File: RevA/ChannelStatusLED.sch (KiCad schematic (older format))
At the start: 6 parts, among them Q1 MBT3946DW1T1, Q2 MBT3946DW1T1, U1 RAx4_4 1K, U2 RAx4_4 1K

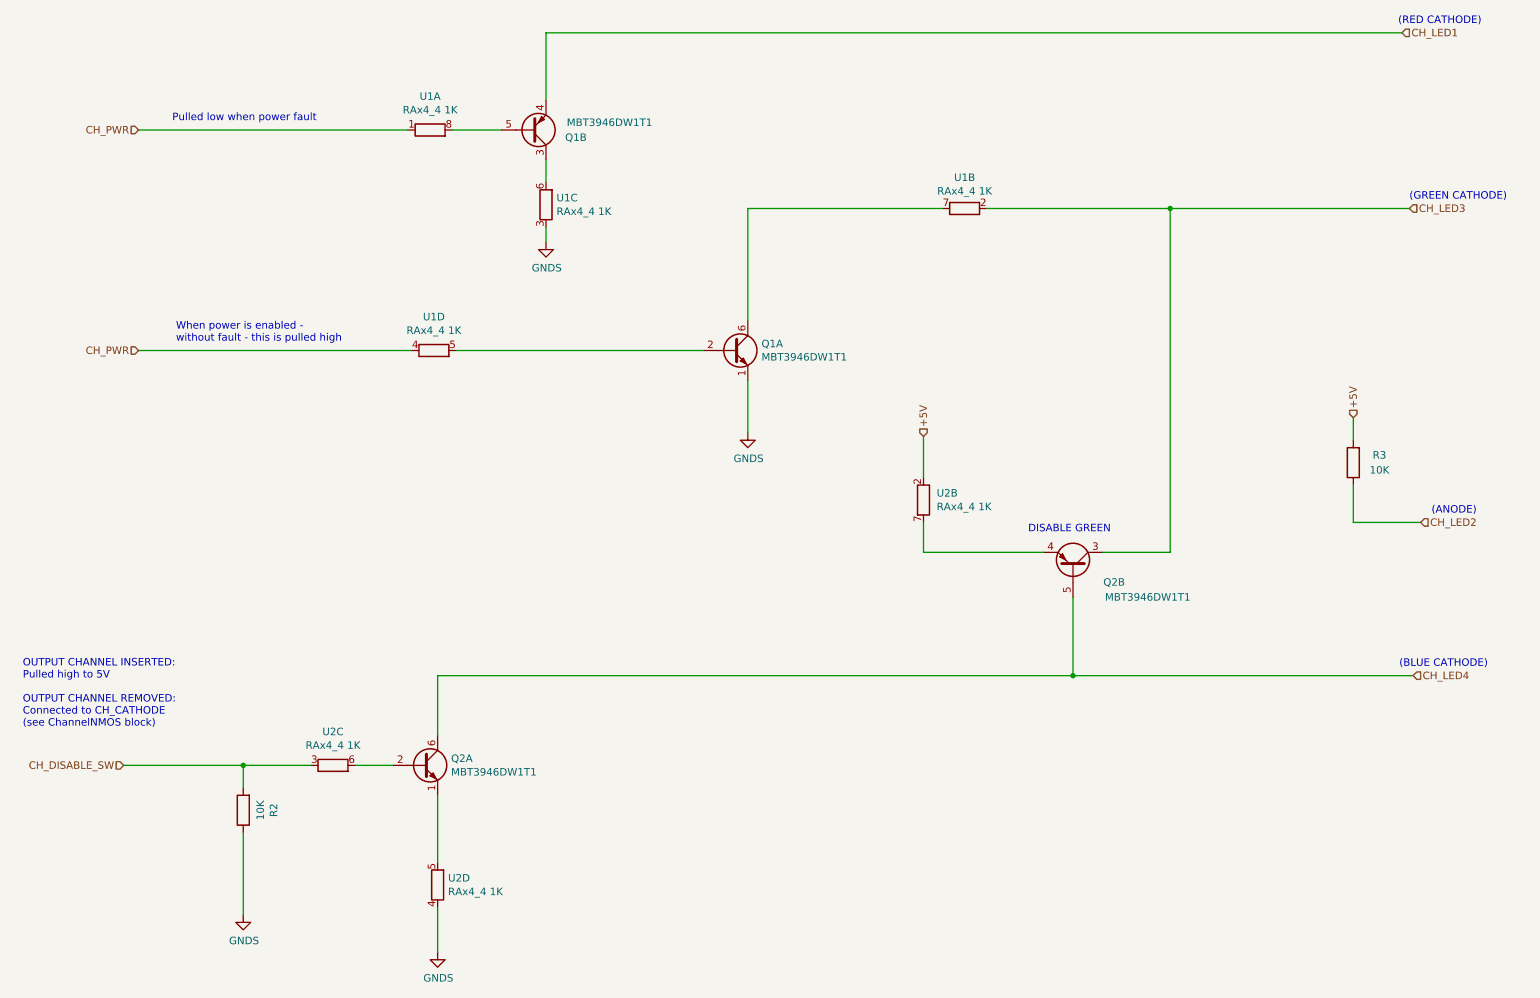
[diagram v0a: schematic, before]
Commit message: updated HW
changed single gang PTD901 to dual gang concentric PTH901
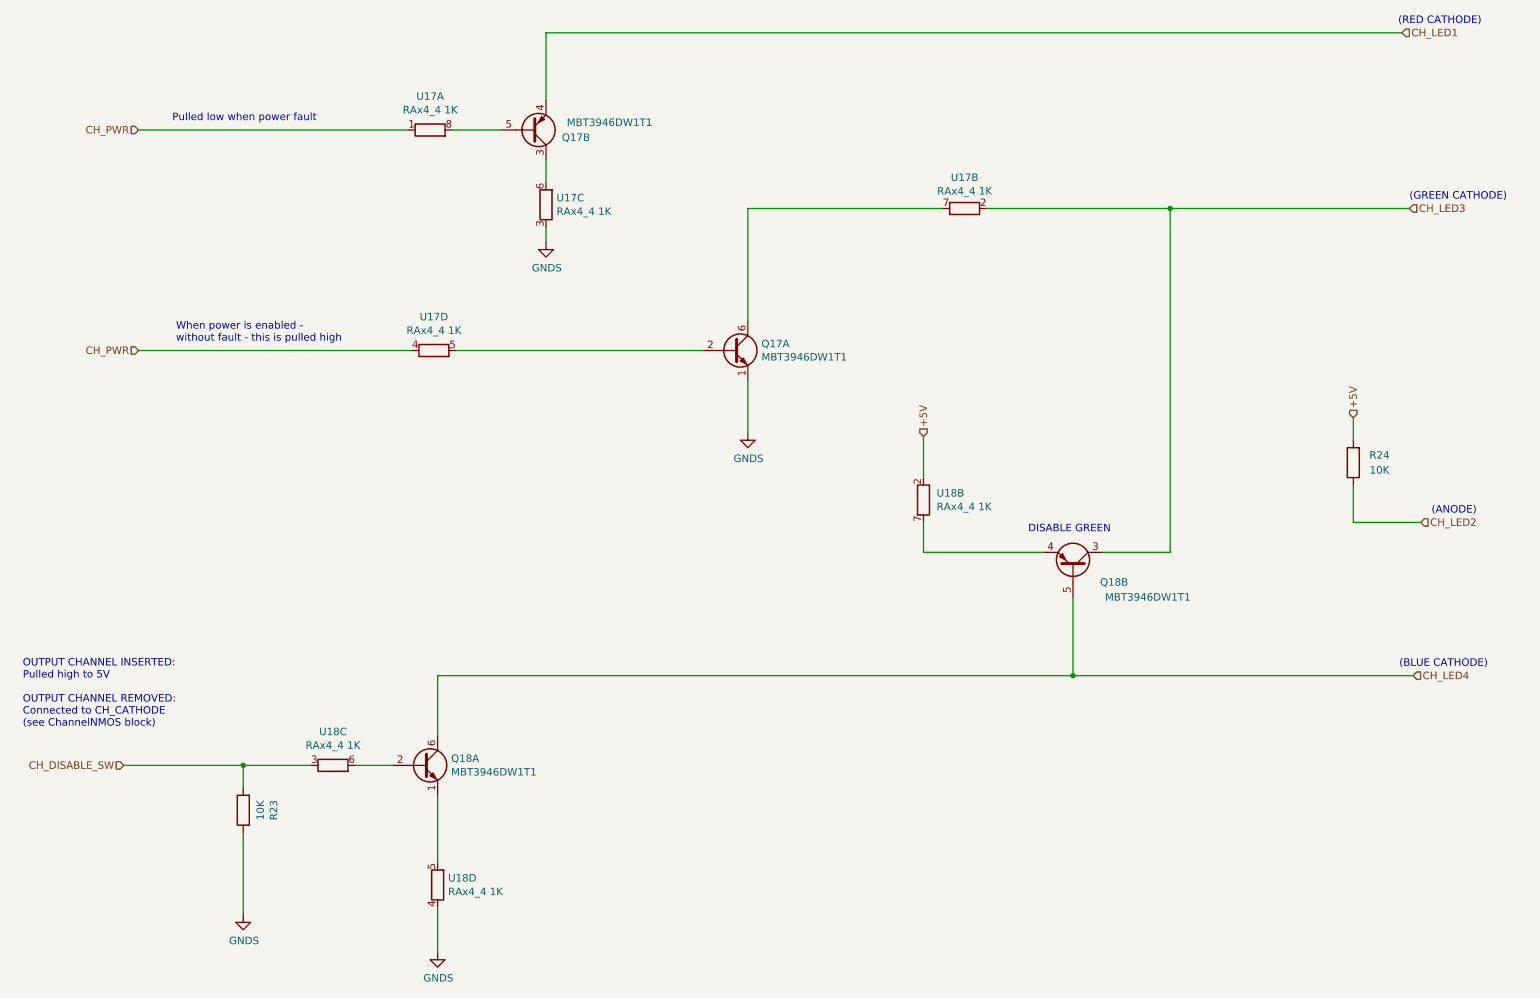
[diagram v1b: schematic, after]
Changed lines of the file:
@@
 AR Path="/5DDA78A9/5DFDF4A8" Ref="Q15"  Part="2"
 AR Path="/5DDBFE07/5DFDF4A8" Ref="Q17"  Part="2"
-F 0 "Q1" H 4575 1950 50  0000 C CNN
+F 0 "Q17" H 4575 1950 50  0000 C CNN
 F 1 "MBT3946DW1T1" H 4800 1850 50  0000 C CNN
 F 2 "Package_TO_SOT_SMD:SOT-363_SC-70-6" H 4475 2000 50  0001 C CNN
@@
 AR Path="/5DDA78A9/5DFDE96B" Ref="Q15"  Part="1"
 AR Path="/5DDBFE07/5DFDE96B" Ref="Q17"  Part="1"
-F 0 "Q1" H 5816 3420 50  0000 L CNN
+F 0 "Q17" H 5816 3420 50  0000 L CNN
 F 1 "MBT3946DW1T1" H 5816 3331 50  0000 L CNN
 F 2 "Package_TO_SOT_SMD:SOT-363_SC-70-6" H 5825 3475 50  0001 C CNN
@@
 AR Path="/5DDA78A9/5DEB0CC3" Ref="#PWR097"  Part="1"
 AR Path="/5DDBFE07/5DEB0CC3" Ref="#PWR099"  Part="1"
-F 0 "#PWR013" H 5725 3675 50  0001 C CNN
+F 0 "#PWR099" H 5725 3675 50  0001 C CNN
 F 1 "GNDS" H 5730 3752 50  0000 C CNN
 F 2 "" H 5725 3925 50  0001 C CNN
@@
 AR Path="/5DDA78A9/5E699B7E" Ref="#PWR035"  Part="1"
 AR Path="/5DDBFE07/5E699B7E" Ref="#PWR037"  Part="1"
-F 0 "#PWR07" H 4375 2400 50  0001 C CNN
+F 0 "#PWR037" H 4375 2400 50  0001 C CNN
 F 1 "GNDS" H 4380 2477 50  0000 C CNN
 F 2 "" H 4375 2650 50  0001 C CNN
@@
 AR Path="/5DDA78A9/5E815CA3" Ref="Q16"  Part="1"
 AR Path="/5DDBFE07/5E815CA3" Ref="Q18"  Part="1"
-F 0 "Q2" H 3740 6196 50  0000 L CNN
+F 0 "Q18" H 3740 6196 50  0000 L CNN
 F 1 "MBT3946DW1T1" H 3740 6105 50  0000 L CNN
 F 2 "Package_TO_SOT_SMD:SOT-363_SC-70-6" H 3750 6250 50  0001 C CNN
@@
 AR Path="/5DDA78A9/5E81663D" Ref="Q16"  Part="2"
 AR Path="/5DDBFE07/5E81663D" Ref="Q18"  Part="2"
-F 0 "Q2" V 7800 5100 50  0000 C CNN
+F 0 "Q18" V 7800 5100 50  0000 C CNN
 F 1 "MBT3946DW1T1" V 7700 5325 50  0000 C CNN
 F 2 "Package_TO_SOT_SMD:SOT-363_SC-70-6" H 8100 4925 50  0001 C CNN
@@
 AR Path="/5DDA78A9/5E819F8C" Ref="#PWR034"  Part="1"
 AR Path="/5DDBFE07/5E819F8C" Ref="#PWR036"  Part="1"
-F 0 "#PWR02" H 3650 7150 50  0001 C CNN
+F 0 "#PWR036" H 3650 7150 50  0001 C CNN
 F 1 "GNDS" H 3655 7227 50  0000 C CNN
 F 2 "" H 3650 7400 50  0001 C CNN
@@
 AR Path="/5DDA78A9/5E833FE4" Ref="R22"  Part="1"
 AR Path="/5DDBFE07/5E833FE4" Ref="R24"  Part="1"
-F 0 "R3" H 9600 4075 50  0000 C CNN
+F 0 "R24" H 9600 4075 50  0000 C CNN
 F 1 "10K" H 9600 4175 50  0000 C CNN
 F 2 "Resistor_SMD:R_0805_2012Metric_Pad1.15x1.40mm_HandSolder" V 9705 4125 50  0001 C CNN
@@
 AR Path="/5DDA78A9/5E846344" Ref="R21"  Part="1"
 AR Path="/5DDBFE07/5E846344" Ref="R23"  Part="1"
-F 0 "R2" V 2146 6450 50  0000 C CNN
+F 0 "R23" V 2146 6450 50  0000 C CNN
 F 1 "10K" V 2235 6450 50  0000 C CNN
 F 2 "Resistor_SMD:R_0805_2012Metric_Pad1.15x1.40mm_HandSolder" V 2280 6450 50  0001 C CNN
@@
 AR Path="/5DDA78A9/5E9652F8" Ref="U15"  Part="1"
 AR Path="/5DDBFE07/5E9652F8" Ref="U17"  Part="1"
-F 0 "U1" H 3600 2125 50  0000 C CNN
+F 0 "U17" H 3600 2125 50  0000 C CNN
 F 1 "RAx4_4 1K" H 3600 2034 50  0000 C CNN
 F 2 "Resistor_SMD:R_Array_Convex_4x0603" H 3600 1800 50  0001 C CNN
@@
 AR Path="/5DDA78A9/5E9687B5" Ref="U15"  Part="2"
 AR Path="/5DDBFE07/5E9687B5" Ref="U17"  Part="2"
-F 0 "U1" H 7175 2218 50  0000 C CNN
+F 0 "U17" H 7175 2218 50  0000 C CNN
 F 1 "RAx4_4 1K" H 7175 2309 50  0000 C CNN
 F 2 "Resistor_SMD:R_Array_Convex_4x0603" H 7175 2325 50  0001 C CNN
@@
 AR Path="/5DDA78A9/5E96B96B" Ref="U15"  Part="3"
 AR Path="/5DDBFE07/5E96B96B" Ref="U17"  Part="3"
-F 0 "U1" V 4421 2330 50  0000 R CNN
+F 0 "U17" V 4421 2330 50  0000 R CNN
 F 1 "RAx4_4 1K" V 4330 2330 50  0000 R CNN
 F 2 "Resistor_SMD:R_Array_Convex_4x0603" H 4375 2300 50  0001 C CNN
@@
 AR Path="/5DDA78A9/5E96FE7B" Ref="U15"  Part="4"
 AR Path="/5DDBFE07/5E96FE7B" Ref="U17"  Part="4"
-F 0 "U1" H 3625 3600 50  0000 C CNN
+F 0 "U17" H 3625 3600 50  0000 C CNN
 F 1 "RAx4_4 1K" H 3625 3509 50  0000 C CNN
 F 2 "Resistor_SMD:R_Array_Convex_4x0603" H 3625 3275 50  0001 C CNN
@@
 AR Path="/5DDA78A9/5E9776FE" Ref="U16"  Part="2"
 AR Path="/5DDBFE07/5E9776FE" Ref="U18"  Part="2"
-F 0 "U2" V 6854 4463 50  0000 L CNN
+F 0 "U18" V 6854 4463 50  0000 L CNN
 F 1 "RAx4_4 1K" V 6945 4463 50  0000 L CNN
 F 2 "Resistor_SMD:R_Array_Convex_4x0603" H 6900 4275 50  0001 C CNN
@@
 AR Path="/5DDA78A9/5E99998D" Ref="U16"  Part="3"
 AR Path="/5DDBFE07/5E99998D" Ref="U18"  Part="3"
-F 0 "U2" H 2950 6375 50  0000 C CNN
+F 0 "U18" H 2950 6375 50  0000 C CNN
 F 1 "RAx4_4 1K" H 2950 6284 50  0000 C CNN
 F 2 "Resistor_SMD:R_Array_Convex_4x0603" H 2950 6050 50  0001 C CNN
@@
 AR Path="/5DDA78A9/5EAAD0E5" Ref="U16"  Part="4"
 AR Path="/5DDBFE07/5EAAD0E5" Ref="U18"  Part="4"
-F 0 "U2" V 3696 6880 50  0000 R CNN
+F 0 "U18" V 3696 6880 50  0000 R CNN
 F 1 "RAx4_4 1K" V 3605 6880 50  0000 R CNN
 F 2 "Resistor_SMD:R_Array_Convex_4x0603" H 3650 6850 50  0001 C CNN
@@
 OUTPUT CHANNEL INSERTED:\nPulled high to 5V\n\nOUTPUT CHANNEL REMOVED:\nConnected to CH_CATHODE \n(see ChannelNMOS block)
 $Comp
-L power:GNDS #PWR?
+L power:GNDS #PWR0115
 U 1 1 5E033493
 P 2350 7150
-AR Path="/5DC5ACCB/5E033493" Ref="#PWR?"  Part="1"
-AR Path="/5DCAAEC9/5E033493" Ref="#PWR?"  Part="1"
-AR Path="/5DD023EE/5E033493" Ref="#PWR?"  Part="1"
-AR Path="/5DD17EF0/5E033493" Ref="#PWR?"  Part="1"
-AR Path="/5DD2E49D/5E033493" Ref="#PWR?"  Part="1"
-AR Path="/5DD6F559/5E033493" Ref="#PWR?"  Part="1"
-AR Path="/5DD8CFA7/5E033493" Ref="#PWR?"  Part="1"
-AR Path="/5DDA78A9/5E033493" Ref="#PWR?"  Part="1"
-AR Path="/5DDBFE07/5E033493" Ref="#PWR?"  Part="1"
-F 0 "#PWR?" H 2350 6900 50  0001 C CNN
+AR Path="/5DC5ACCB/5E033493" Ref="#PWR0115"  Part="1"
+AR Path="/5DCAAEC9/5E033493" Ref="#PWR0120"  Part="1"
+AR Path="/5DD023EE/5E033493" Ref="#PWR0123"  Part="1"
+AR Path="/5DD17EF0/5E033493" Ref="#PWR0131"  Part="1"
+AR Path="/5DD2E49D/5E033493" Ref="#PWR0140"  Part="1"
+AR Path="/5DD6F559/5E033493" Ref="#PWR0147"  Part="1"
+AR Path="/5DD8CFA7/5E033493" Ref="#PWR0148"  Part="1"
+AR Path="/5DDA78A9/5E033493" Ref="#PWR0149"  Part="1"
+AR Path="/5DDBFE07/5E033493" Ref="#PWR0150"  Part="1"
+F 0 "#PWR0150" H 2350 6900 50  0001 C CNN
 F 1 "GNDS" H 2355 6977 50  0000 C CNN
 F 2 "" H 2350 7150 50  0001 C CNN

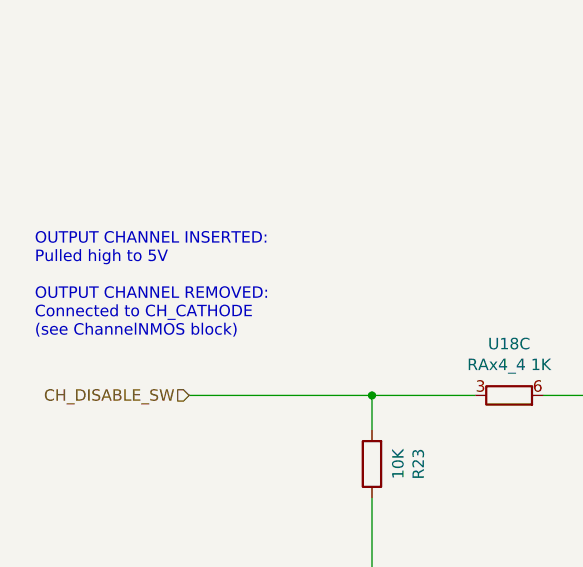
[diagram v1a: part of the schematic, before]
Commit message: Added some annotations to schematic
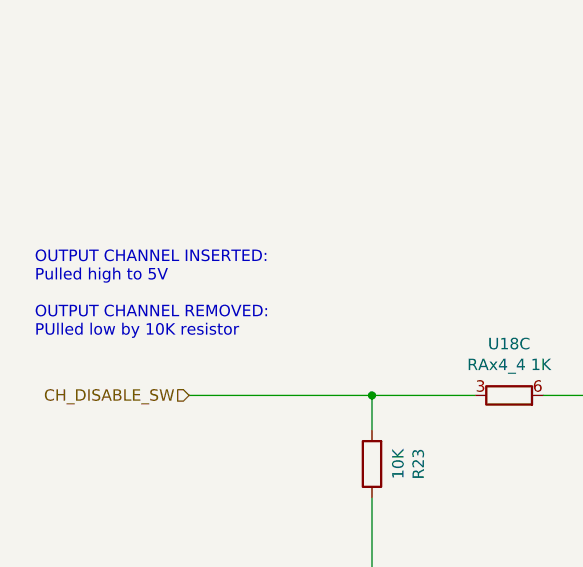
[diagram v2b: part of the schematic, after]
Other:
- note added: "OUTPUT CHANNEL INSERTED:\nPulled high to 5V\n\nOUTPUT CHANNEL REMOVED:\nPUlled low by 10K resistor"
- note removed: "OUTPUT CHANNEL INSERTED:\nPulled high to 5V\n\nOUTPUT CHANNEL REMOVED:\nConnected to CH_CATHODE \n(see ChannelNMOS block)"
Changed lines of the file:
@@
 $Descr A4 11693 8268
 encoding utf-8
-Sheet 2 29
+Sheet 10 29
 Title ""
 Date ""
@@
 	1650 1900 3450 1900
 Text Notes 875  5900 0    50   ~ 0
-OUTPUT CHANNEL INSERTED:\nPulled high to 5V\n\nOUTPUT CHANNEL REMOVED:\nConnected to CH_CATHODE \n(see ChannelNMOS block)
+OUTPUT CHANNEL INSERTED:\nPulled high to 5V\n\nOUTPUT CHANNEL REMOVED:\nPUlled low by 10K resistor
 $Comp
 L power:GNDS #PWR0115
